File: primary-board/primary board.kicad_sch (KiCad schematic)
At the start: 28 parts, among them J1 USB_C, J10 Motor Connector Right, J9 Motor Connector Left, SW1 SW_SPST, SW2 SW_SPST, U1 ESP32-S3-1, U5 DRV8411ARTER

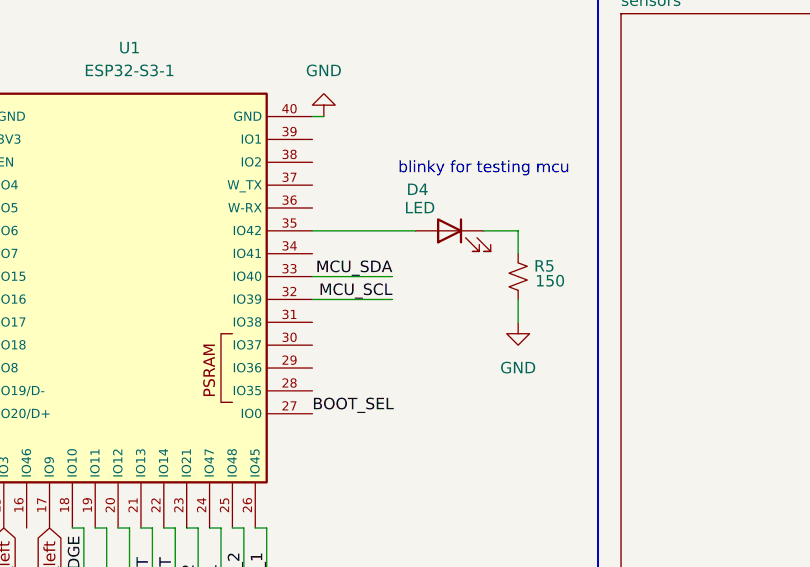
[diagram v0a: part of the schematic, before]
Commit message: routed analog sensors
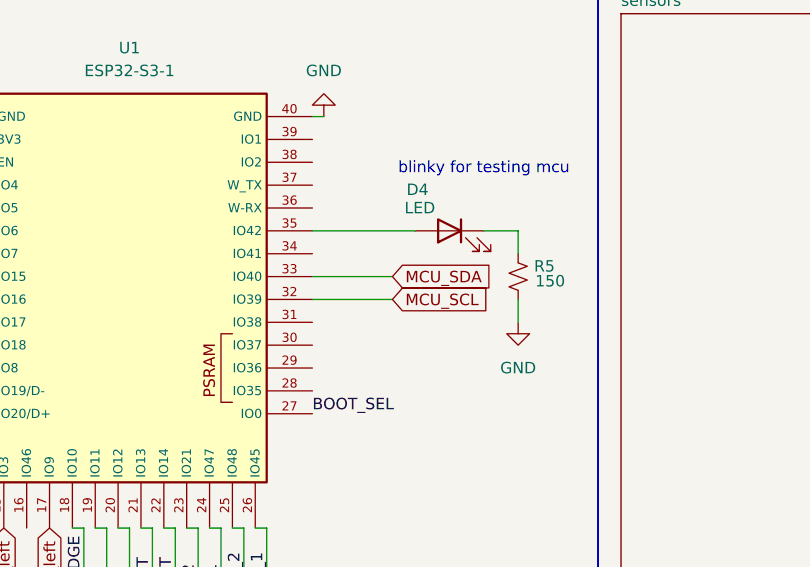
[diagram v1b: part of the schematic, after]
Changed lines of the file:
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@@
-		)
-	)
-	(label "MCU_SCL"
-		(at 201.93 58.42 180)
-		(effects
-			(font
-				(size 1.27 1.27)
-			)
-			(justify right bottom)
 		)
 	)
@@
 		)
 	)
-	(label "MCU_SDA"
-		(at 201.93 55.88 180)
-		(effects
-			(font
-				(size 1.27 1.27)
-			)
-			(justify right bottom)
-		)
-	)
 	(label "M1_LEFT"
 		(at 128.27 124.46 180)
@@
 		)
 	)
+	(global_label "MCU_SDA"
+		(shape input)
+		(at 201.93 55.88 0)
+		(fields_autoplaced yes)
+		(effects
+			(font
+				(size 1.27 1.27)
+			)
+			(justify left)
+		)
+		(property "Intersheetrefs" "${INTERSHEET_REFS}"
+			(at 213.5028 55.88 0)
+			(effects
+				(font
+					(size 1.27 1.27)
+				)
+				(justify left)
+				(hide yes)
+			)
+		)
+	)
 	(global_label "ir_led_right"
 		(shape input)
@@
 				(hide yes)
 			)
+		)
+	)
+	(global_label "MCU_SCL"
+		(shape input)
+		(at 201.93 58.42 0)
+		(fields_autoplaced yes)
+		(effects
+			(font
+				(size 1.27 1.27)
+			)
+			(justify left)
+		)
+		(property "Intersheetrefs" "${INTERSHEET_REFS}"
+			(at 213.4423 58.42 0)
+			(effects
+				(font
+					(size 1.27 1.27)
+				)
+				(justify left)
+				(hide yes)
+			)
